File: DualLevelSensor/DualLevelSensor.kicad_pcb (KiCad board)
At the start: 4 copper layers, 40 x 100 mm, 90 parts, among them J1 USB_B_Micro, J2 Conn_01x03, J3 Conn_01x03, J4 Conn_01x03, J5 Conn_01x02, K1 capPad, K10 capPad, K11 capPad, K12 capPad, K13 capPad, K14 capPad, K15 capPad, K16 capPad, K17 capPad, K18 capPad, K19 capPad, K2 capPad, K20 capPad, K21 capPad, K22 capPad, K3 capPad, K4 capPad, K5 capPad, K6 capPad, K7 capPad, K8 capPad, K9 capPad, U1 W25Q16JVUXIQ, U2 RP2040, U3 AP63357Q, Y1 12Mhz

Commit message: wip
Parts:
- added R35: 10R, Resistor_SMD:R_0603_1608Metric, B.Cu at (106.7, 32.9)
- added R36: 10R, Resistor_SMD:R_0603_1608Metric, B.Cu at (105.5, 32.9)
- C13, C17: value 100nF -> 1µF
- D1: moved to F.Cu
- moved R33 4.21 mm to (114.0, 36.1)
- moved D1 3.44 mm to (109.8, 34.5), turned to -90 degrees
- moved R2 0.25 mm to (103.3, 33.8)
- moved R3 0.25 mm to (103.3, 32.6)
- moved R10 0.10 mm to (103.1, 30.8)
- moved R9 0.10 mm to (106.0, 30.8)
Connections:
- D1 pad 2: VBUS -> Net-(D1-Pad2)
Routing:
- net Net-(D1-Pad2): track 0.00 -> 5.22 mm, vias 0 -> 1
- net /UART1: track 15.7 -> 19.0 mm
- net +24V: track 45.2 -> 42.1 mm
- net VBUS: track 3.40 -> 4.92 mm
- net GND: track 51.6 -> 52.4 mm

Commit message: wip
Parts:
- added L2: 1µ, Inductor_SMD:L_0805_2012Metric, F.Cu at (80.4, 34.7)
- moved R34 4.24 mm to (76.1, 36.6)
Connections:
- C6 pad 2: +24V -> Net-(C6-Pad2)
- U3 pad 1: +24V -> Net-(C6-Pad2)
- U3 pad 2: +24V -> Net-(C6-Pad2)
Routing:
- net +24V: track 42.1 -> 44.0 mm
- net /UART0: track 25.3 -> 27.1 mm
- net Net-(C6-Pad2): track 0.00 -> 1.09 mm
- net Net-(J4-Pad3): track 2.85 -> 2.35 mm
- added copper zone on F.Cu, net Net-(C6-Pad2)
- removed copper zone on F.Cu, net +24V

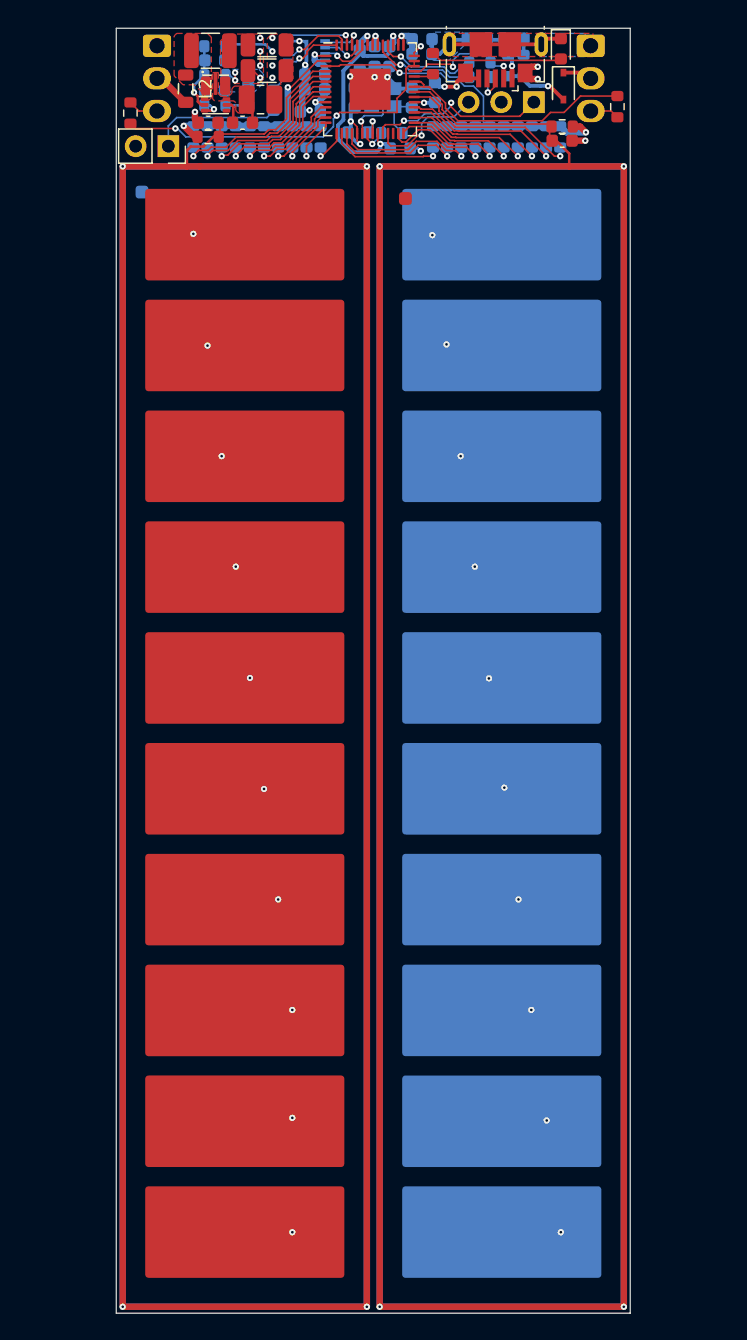
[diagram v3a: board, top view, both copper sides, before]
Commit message: added fluidsensor
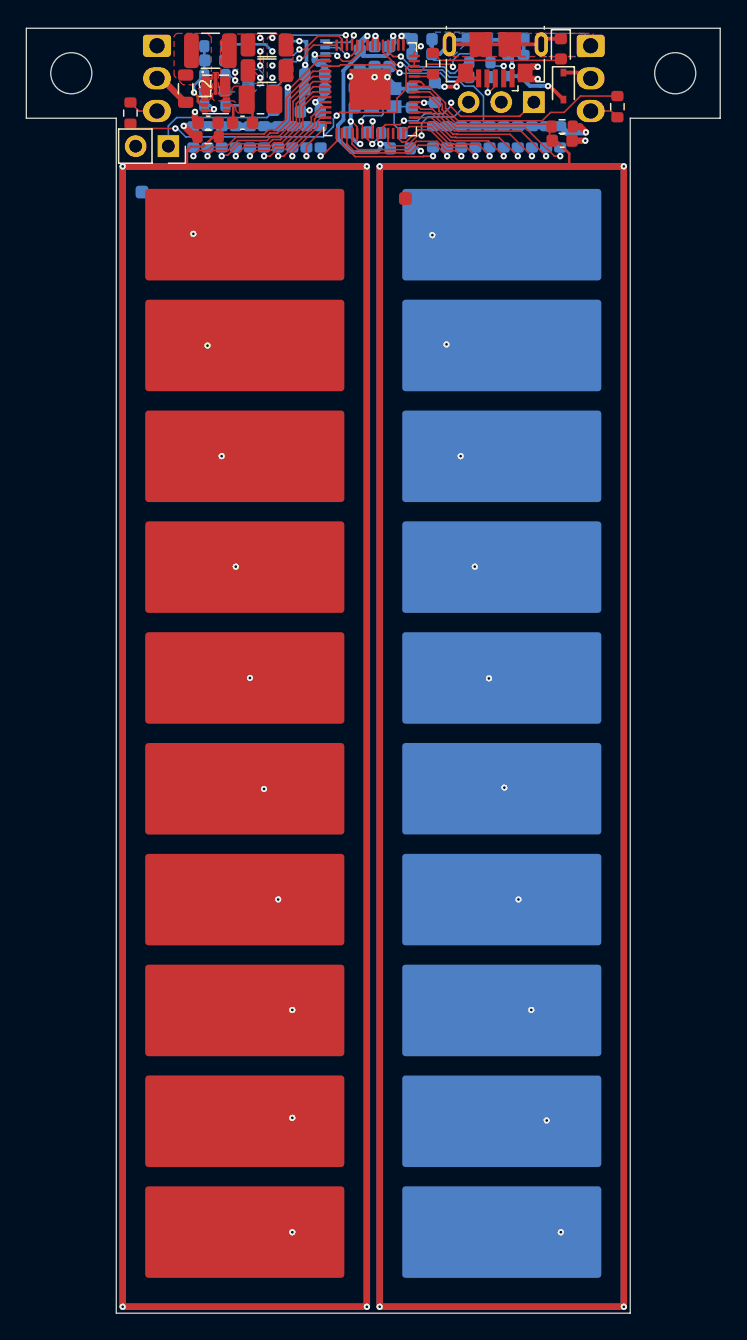
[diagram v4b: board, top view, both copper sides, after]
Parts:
- added H1: MountingHole, MountingHole:MountingHole_3.2mm_M3_DIN965, F.Cu at (118.5, 33.5)
- added H2: MountingHole, MountingHole:MountingHole_3.2mm_M3_DIN965, F.Cu at (71.5, 33.5)
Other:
- board size 40 x 100 mm -> 54 x 100 mm
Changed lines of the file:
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@@
       (net 29 "/+sens7") (pinfunction "Pin_1") (pintype "passive"))
+  )
+  (footprint "MountingHole:MountingHole_3.2mm_M3_DIN965" (layer "F.Cu")
+    (at 71.5 33.5)
+    (descr "Mounting Hole 3.2mm, no annular, M3, DIN965")
+    (tags "mounting hole 3.2mm no annular m3 din965")
+    (property "Sheetfile" "DualLevelSensor.kicad_sch")
+    (property "Sheetname" "")
+    (attr exclude_from_pos_files)
+    (fp_text reference "H2" (at 0 -3.8) (layer "F.SilkS") hide
+      (effects (font (size 1 1) (thickness 0.15)))
+    )
+    (fp_text value "MountingHole" (at 0 3.8) (layer "F.Fab")
+      (effects (font (size 1 1) (thickness 0.15)))
+    )
+    (fp_text user "${REFERENCE}" (at 0 0) (layer "F.Fab")
+      (effects (font (size 1 1) (thickness 0.15)))
+    )
+    (fp_circle (center 0 0) (end 2.8 0) (layer "Cmts.User") (width 0.15) (fill none))
+    (fp_circle (center 0 0) (end 3.05 0) (layer "F.CrtYd") (width 0.05) (fill none))
+    (pad "" np_thru_hole circle (at 0 0) (size 3.2 3.2) (drill 3.2) (layers *.Cu *.Mask))
   )
   (footprint "Capacitor_SMD:C_1206_3216Metric" (layer "F.Cu")
@@
     (pad "1" smd roundrect (at 0 0) (size 15.5 7.125) (layers "F.Cu") (roundrect_rratio 0.0350877193)
       (net 24 "/+sens2") (pinfunction "Pin_1") (pintype "passive"))
+  )
+  (footprint "MountingHole:MountingHole_3.2mm_M3_DIN965" (layer "F.Cu")
+    (at 118.5 33.5)
+    (descr "Mounting Hole 3.2mm, no annular, M3, DIN965")
+    (tags "mounting hole 3.2mm no annular m3 din965")
+    (property "Sheetfile" "DualLevelSensor.kicad_sch")
+    (property "Sheetname" "")
+    (attr exclude_from_pos_files)
+    (fp_text reference "H1" (at 0 -3.8) (layer "F.SilkS") hide
+      (effects (font (size 1 1) (thickness 0.15)))
+    )
+    (fp_text value "MountingHole" (at 0 3.8) (layer "F.Fab")
+      (effects (font (size 1 1) (thickness 0.15)))
+    )
+    (fp_text user "${REFERENCE}" (at 0 0) (layer "F.Fab")
+      (effects (font (size 1 1) (thickness 0.15)))
+    )
+    (fp_circle (center 0 0) (end 2.8 0) (layer "Cmts.User") (width 0.15) (fill none))
+    (fp_circle (center 0 0) (end 3.05 0) (layer "F.CrtYd") (width 0.05) (fill none))
+    (pad "" np_thru_hole circle (at 0 0) (size 3.2 3.2) (drill 3.2) (layers *.Cu *.Mask))
   )
   (footprint "Resistor_SMD:R_0603_1608Metric" (layer "F.Cu")
@@
   )
   (gr_line (start 95 30) (end 95 130) (layer "Dwgs.User") (width 0.1))
-  (gr_line (start 115 30) (end 115 130) (layer "Edge.Cuts") (width 0.1))
-  (gr_line (start 75 30) (end 115 30) (layer "Edge.Cuts") (width 0.1))
+  (gr_line (start 122 30) (end 122 37) (layer "Edge.Cuts") (width 0.1))
+  (gr_line (start 115 37) (end 115 130) (layer "Edge.Cuts") (width 0.1))
+  (gr_line (start 68 30) (end 122 30) (layer "Edge.Cuts") (width 0.1))
+  (gr_line (start 68 37) (end 75 37) (layer "Edge.Cuts") (width 0.1))
   (gr_line (start 75 130) (end 115 130) (layer "Edge.Cuts") (width 0.1))
-  (gr_line (start 75 30) (end 75 130) (layer "Edge.Cuts") (width 0.1))
+  (gr_line (start 122 37) (end 115 37) (layer "Edge.Cuts") (width 0.1))
+  (gr_line (start 68 30) (end 68 37) (layer "Edge.Cuts") (width 0.1))
+  (gr_line (start 75 37) (end 75 130) (layer "Edge.Cuts") (width 0.1))
   (dimension (type aligned) (layer "Dwgs.User")
     (pts (xy 75 40.25) (xy 75 30))

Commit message: prepare for Manufacturing
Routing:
- net +24V: track 44.0 -> 43.4 mm
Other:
- outline, holes or cut-outs redrawn
- board text added: "DualLevelSensor V1.0"
